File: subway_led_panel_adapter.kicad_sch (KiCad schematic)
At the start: 51 parts, among them J1 Conn_02x06_Odd_Even, J2 Conn_02x10_Odd_Even, J3 Conn_02x06_Odd_Even, J4 Conn_02x20_Odd_Even, J5 Conn_02x06_Odd_Even, U1 74AHCT244, U2 ChinaBluePill, U3 74LVC1G123, U4 74LVC1GU04DRL

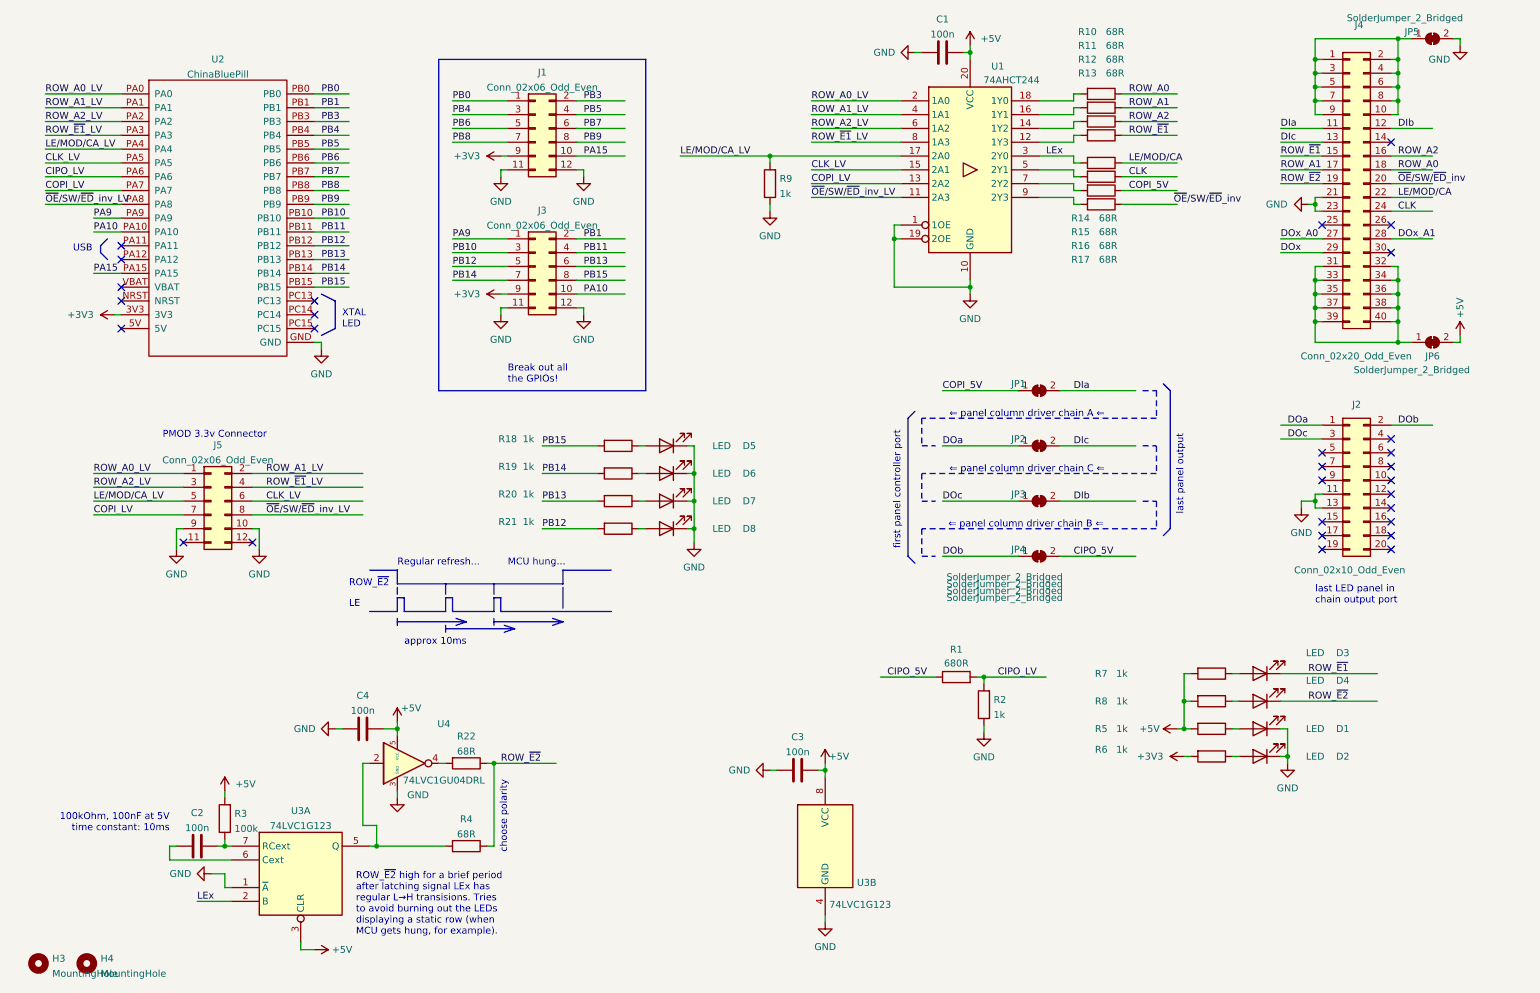
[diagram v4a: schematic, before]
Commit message: Start working on Rev. B: Adds 3v3 Regulator
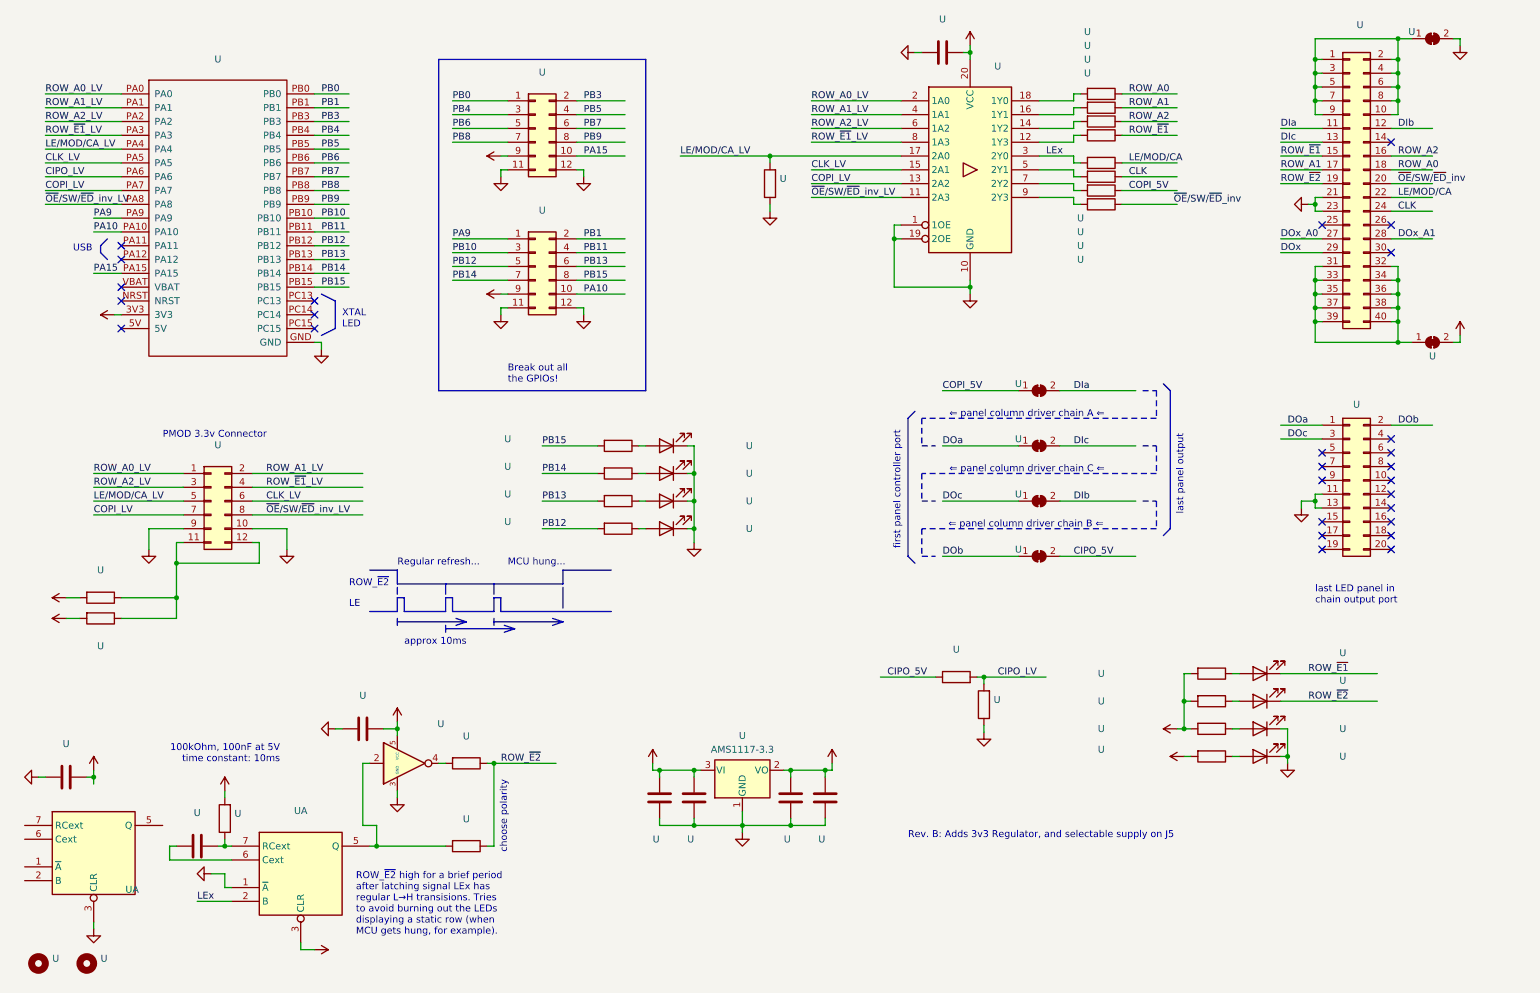
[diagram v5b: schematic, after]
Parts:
- added U (x4): (no value), symbol Device:C
- added U (x2): (no value), symbol Device:R
- added U: AMS1117-3.3, Package_TO_SOT_SMD:SOT-223-3_TabPin2, symbol Regulator_Linear:AMS1117-3.3
- U: renamed from D8; value LED -> (none); footprint LED_SMD:LED_0603_1608Metric -> (none)
- U: renamed from R17; value 68R -> (none); footprint Resistor_SMD:R_0603_1608Metric -> (none)
- U: renamed from C4; value 100n -> (none); footprint Capacitor_SMD:C_0603_1608Metric -> (none)
- U: renamed from R5; value 1k -> (none); footprint Resistor_SMD:R_0603_1608Metric -> (none)
- U: renamed from J4; value Conn_02x20_Odd_Even -> (none); footprint Connector_PinSocket_2.54mm:PinSocket_2x20_P2.54mm_Vertical -> (none)
- U: renamed from R10; value 68R -> (none); footprint Resistor_SMD:R_0603_1608Metric -> (none)
- U: renamed from JP1; value SolderJumper_2_Bridged -> (none); footprint Jumper:SolderJumper-2_P1.3mm_Bridged_Pad1.0x1.5mm -> (none)
- U: renamed from JP6; value SolderJumper_2_Bridged -> (none); footprint Jumper:SolderJumper-2_P1.3mm_Bridged_Pad1.0x1.5mm -> (none)
- U: renamed from R4; value 68R -> (none); footprint Resistor_SMD:R_0603_1608Metric -> (none)
- U: renamed from C1; value 100n -> (none); footprint Capacitor_SMD:C_0603_1608Metric -> (none)
- U: renamed from R21; value 1k -> (none); footprint Resistor_SMD:R_0603_1608Metric -> (none)
- U: renamed from JP5; value SolderJumper_2_Bridged -> (none); footprint Jumper:SolderJumper-2_P1.3mm_Bridged_Pad1.0x1.5mm -> (none)
- U: renamed from C2; value 100n -> (none); footprint Capacitor_SMD:C_0603_1608Metric -> (none)
- U: renamed from JP3; value SolderJumper_2_Bridged -> (none); footprint Jumper:SolderJumper-2_P1.3mm_Bridged_Pad1.0x1.5mm -> (none)
- U: renamed from R13; value 68R -> (none); footprint Resistor_SMD:R_0603_1608Metric -> (none)
- U: renamed from R14; value 68R -> (none); footprint Resistor_SMD:R_0603_1608Metric -> (none)
- U: renamed from R11; value 68R -> (none); footprint Resistor_SMD:R_0603_1608Metric -> (none)
- U: renamed from R15; value 68R -> (none); footprint Resistor_SMD:R_0603_1608Metric -> (none)
- U: renamed from R19; value 1k -> (none); footprint Resistor_SMD:R_0603_1608Metric -> (none)
- U: renamed from H3; value MountingHole -> (none); footprint MountingHole:MountingHole_4.3mm_M4 -> (none)
- U: renamed from J5; value Conn_02x06_Odd_Even -> (none); footprint Connector_PinHeader_2.54mm:PinHeader_2x06_P2.54mm_Vertical -> (none)
- U: renamed from U4; value 74LVC1GU04DRL -> (none); footprint Package_TO_SOT_SMD:SOT-553 -> (none)
- U: renamed from JP4; value SolderJumper_2_Bridged -> (none); footprint Jumper:SolderJumper-2_P1.3mm_Bridged_Pad1.0x1.5mm -> (none)
- U: renamed from R7; value 1k -> (none); footprint Resistor_SMD:R_0603_1608Metric -> (none)
- U: renamed from J2; value Conn_02x10_Odd_Even -> (none); footprint Connector_PinHeader_2.54mm:PinHeader_2x10_P2.54mm_Vertical -> (none)
- U: renamed from C3; value 100n -> (none); footprint Capacitor_SMD:C_0603_1608Metric -> (none)
- U: renamed from R9; value 1k -> (none); footprint Resistor_SMD:R_0603_1608Metric -> (none)
- U: renamed from D1; value LED -> (none); footprint LED_SMD:LED_0603_1608Metric -> (none)
- U: renamed from R1; value 680R -> (none); footprint Resistor_SMD:R_0603_1608Metric -> (none)
- U: renamed from D3; value LED -> (none); footprint LED_SMD:LED_0603_1608Metric -> (none)
- U: renamed from U3; value 74LVC1G123 -> (none); footprint Package_SO:SSOP-8_2.95x2.8mm_P0.65mm -> (none)
- U: renamed from R2; value 1k -> (none); footprint Resistor_SMD:R_0603_1608Metric -> (none)
- U: renamed from JP2; value SolderJumper_2_Bridged -> (none); footprint Jumper:SolderJumper-2_P1.3mm_Bridged_Pad1.0x1.5mm -> (none)
- U: renamed from D4; value LED -> (none); footprint LED_SMD:LED_0603_1608Metric -> (none)
- U: renamed from D2; value LED -> (none); footprint LED_SMD:LED_0603_1608Metric -> (none)
- U: renamed from R18; value 1k -> (none); footprint Resistor_SMD:R_0603_1608Metric -> (none)
- U: renamed from U2; value ChinaBluePill -> (none); footprint chinabluepill:ChinaBluePill -> (none)
- U: renamed from R3; value 100k -> (none); footprint Resistor_SMD:R_0603_1608Metric -> (none)
- U: renamed from R12; value 68R -> (none); footprint Resistor_SMD:R_0603_1608Metric -> (none)
- U: renamed from U1; value 74AHCT244 -> (none); footprint Package_SO:SSOP-20_4.4x6.5mm_P0.65mm -> (none)
- U: renamed from D5; value LED -> (none); footprint LED_SMD:LED_0603_1608Metric -> (none)
- U: renamed from D7; value LED -> (none); footprint LED_SMD:LED_0603_1608Metric -> (none)
- U: renamed from D6; value LED -> (none); footprint LED_SMD:LED_0603_1608Metric -> (none)
- U: renamed from R6; value 1k -> (none); footprint Resistor_SMD:R_0603_1608Metric -> (none)
- U: renamed from J1; value Conn_02x06_Odd_Even -> (none); footprint Connector_PinHeader_2.54mm:PinHeader_2x06_P2.54mm_Vertical -> (none)
- U: renamed from R16; value 68R -> (none); footprint Resistor_SMD:R_0603_1608Metric -> (none)
- U: renamed from R22; value 68R -> (none); footprint Resistor_SMD:R_0603_1608Metric -> (none)
- U: renamed from R20; value 1k -> (none); footprint Resistor_SMD:R_0603_1608Metric -> (none)
- U: renamed from H4; value MountingHole -> (none); footprint MountingHole:MountingHole_4.3mm_M4 -> (none)
- U: renamed from R8; value 1k -> (none); footprint Resistor_SMD:R_0603_1608Metric -> (none)
- U: renamed from J3; value Conn_02x06_Odd_Even -> (none); footprint Connector_PinHeader_2.54mm:PinHeader_2x06_P2.54mm_Vertical -> (none)
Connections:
- net +3V3: now also U.2, U.2, U.2, U.2 (VO)
- net +5V: now also U.2, U.2, U.2, U.3 (VI); no longer U.8 (VCC)
- net GND: now also U.3 (CLR), U.1, U.1, U.1, U.1, U.1 (GND); no longer U.4 (GND)
- net at U.11 (Pin_11): now also U.12 (Pin_12), U.1, U.1
- no-connect marks 29 -> 27
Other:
- note added: "Rev. B: Adds 3v3 Regulator, and selectable supply on J5"
- moved on the sheet: U

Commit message: Cleanup rev. B.
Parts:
- removed U: (no value), symbol Device:R
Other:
- note removed: "choose polarity"
- moved on the sheet: U
